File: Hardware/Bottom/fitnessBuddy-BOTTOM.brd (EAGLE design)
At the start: 33 x 33 mm, 44 parts, among them U1 AD5242-SO16, U4 PCF8523

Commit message: finished routing PPG Board
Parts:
- removed U$4: AD5171, LinnesLab-DigitalIC:SOT-23-8
- added AD5171: AD5171, LinnesLab-DigitalIC:SOT-23-8
- added C4: 100n, LinnesLab-Passives:C0603
- added LOGO1: REVISION.A, LinnesLab-Logos:REV.A
- added LOGO2: OSHW-LOGOS, LinnesLab-Logos:OSHW-LOGO-S
- moved R21 2.70 mm to (32.4, 17.4)
- moved R15 2.39 mm to (32.4, 14.0)
- moved C16 0.78 mm to (34.0, 14.0), turned to 90 degrees
- moved R13 0.30 mm to (33.4, 5.26)
- moved R19 0.30 mm to (33.4, 8.49)
- moved C18 0.18 mm to (6.77, 8.11)
- moved C17 0.16 mm to (8.66, 22.4)
- renumbered OP4 to TIA, U1 to AD5242
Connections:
- net 3.3V: now also AD5171.2, AD5171.6; no longer U$4.2, U$4.6
- net D29/LED.CTRL: now also AD5171.8; no longer U$4.8
- net GND: now also AD5171.3, C4.2; no longer U$4.3
- net N$9: now also AD5171.1, AD5171.7; no longer U$4.1, U$4.7
- net SCL: now also AD5171.4; no longer U$4.4
- net SDA: now also AD5171.5; no longer U$4.5
- net VREF: now also C4.1
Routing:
- net VREF: track 1.27 -> 35.1 mm, vias 0 -> 3
- net N$13: track 4.67 -> 13.9 mm
- net N$16: track 4.05 -> 9.17 mm
- net SCL: track 35.6 -> 39.3 mm
- net A6/TIA: track 64.9 -> 67.0 mm
- net GND: track 25.7 -> 27.6 mm, vias 14 -> 15
- net A7/PPG: track 45.4 -> 47.3 mm
- net N$8: track 0.00 -> 1.71 mm
- net PD.C: track 24.8 -> 24.3 mm

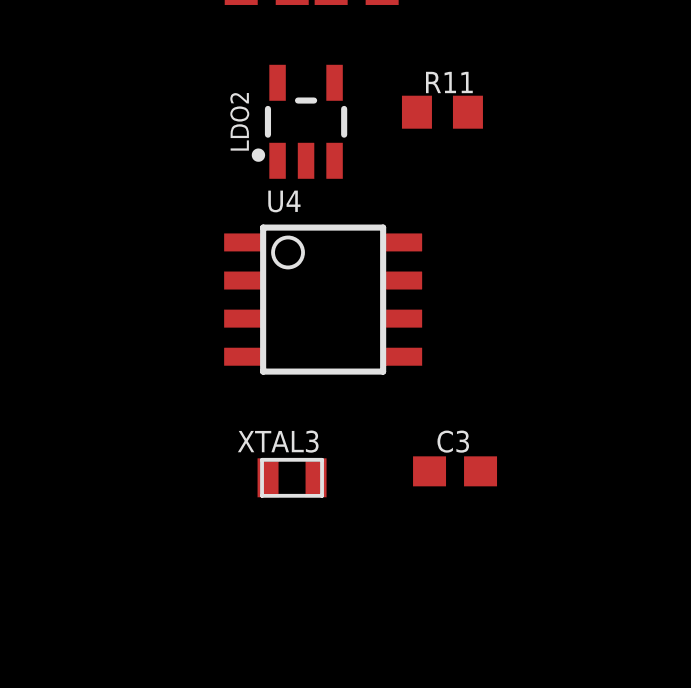
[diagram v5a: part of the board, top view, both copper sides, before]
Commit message: Began routing top board
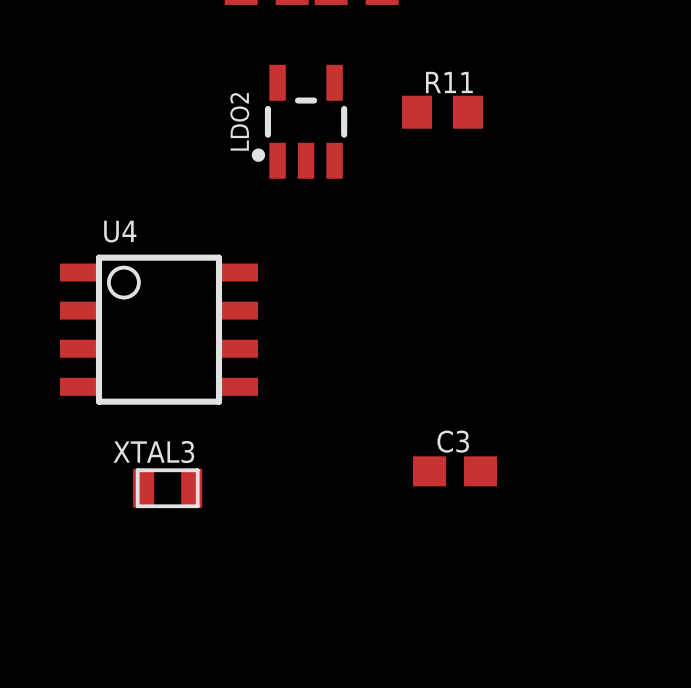
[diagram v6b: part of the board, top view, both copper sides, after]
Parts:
- moved U4 5.56 mm to (-24.3, 18.9)
- moved XTAL3 4.16 mm to (-24.0, 13.6)
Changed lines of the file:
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@@
 <drawing>
 <settings>
-<setting alwaysvectorfont="yes"/>
+<setting alwaysvectorfont="no"/>
 <setting verticaltext="up"/>
 </settings>
@@
 <attribute name="VALUE" x="-15.054578125" y="12.283440625" size="0.7112" layer="27"/>
 </element>
-<element name="XTAL3" library="LinnesLab-Clocks" package="2-SMD.NOLEAD.2.0MMTO1.2MM" package3d_urn="urn:adsk.eagle:package:18579459/2" value="32.7680kHz" x="-19.852640625" y="13.972540625" smashed="yes">
-<attribute name="NAME" x="-21.685040625" y="14.824140625" size="0.7112" layer="25"/>
-<attribute name="VALUE" x="-21.583440625" y="12.277340625" size="0.7112" layer="27"/>
-</element>
-<element name="U4" library="LinnesLab-Clocks" package="SO8" package3d_urn="urn:adsk.eagle:package:18599600/2" value="PCF8523" x="-18.81631875" y="19.9136" smashed="yes">
-<attribute name="DIGIKEY" value="568-5306-1-ND" x="-29.6291" y="23.8506" size="1.778" layer="27" display="off"/>
-<attribute name="I2C_ADDRESS" value="0x68h" x="-29.6291" y="23.8506" size="1.778" layer="27" display="off"/>
-<attribute name="MFN" value="PCF8523T/1,118" x="-29.6291" y="23.8506" size="1.778" layer="27" display="off"/>
-<attribute name="MFN_MANUFACTURER" value="NXP USA Inc." x="-29.6291" y="23.8506" size="1.778" layer="27" display="off"/>
-<attribute name="NAME" x="-20.72131875" y="22.8346" size="0.7112" layer="25"/>
-<attribute name="VALUE" x="-20.72131875" y="16.3576" size="0.7112" layer="27"/>
+<element name="XTAL3" library="LinnesLab-Clocks" package="2-SMD.NOLEAD.2.0MMTO1.2MM" package3d_urn="urn:adsk.eagle:package:18579459/2" value="32.7680kHz" x="-23.997921875" y="13.624559375" smashed="yes">
+<attribute name="NAME" x="-25.830321875" y="14.476159375" size="0.7112" layer="25"/>
+<attribute name="VALUE" x="-25.728721875" y="11.929359375" size="0.7112" layer="27"/>
+</element>
+<element name="U4" library="LinnesLab-Clocks" package="SO8" package3d_urn="urn:adsk.eagle:package:18599600/2" value="PCF8523" x="-24.287478125" y="18.9103" smashed="yes">
+<attribute name="DIGIKEY" value="568-5306-1-ND" x="-35.100259375" y="22.8473" size="1.778" layer="27" display="off"/>
+<attribute name="I2C_ADDRESS" value="0x68h" x="-35.100259375" y="22.8473" size="1.778" layer="27" display="off"/>
+<attribute name="MFN" value="PCF8523T/1,118" x="-35.100259375" y="22.8473" size="1.778" layer="27" display="off"/>
+<attribute name="MFN_MANUFACTURER" value="NXP USA Inc." x="-35.100259375" y="22.8473" size="1.778" layer="27" display="off"/>
+<attribute name="NAME" x="-26.192478125" y="21.8313" size="0.7112" layer="25"/>
+<attribute name="VALUE" x="-26.192478125" y="15.3543" size="0.7112" layer="27"/>
 </element>
 <element name="C4" library="LinnesLab-Passives" package="C0603" package3d_urn="urn:adsk.eagle:package:15661989/2" value="100n" x="28.201625" y="25.68448125" smashed="yes" rot="R90">
@@
 <wire x1="-19.385278125" y1="24.539321875" x2="-15.688678125" y2="26.1594625" width="0" layer="19" extent="1-1"/>
 <wire x1="-21.54591875" y1="30.233621875" x2="-16.84871875" y2="30.233621875" width="0" layer="19" extent="1-1"/>
-<wire x1="-21.46631875" y1="18.0086" x2="-19.385278125" y2="24.539321875" width="0" layer="19" extent="1-1"/>
-<wire x1="-13.569578125" y1="14.188440625" x2="-21.46631875" y2="18.0086" width="0" layer="19" extent="1-1"/>
+<wire x1="-26.937478125" y1="17.0053" x2="-19.385278125" y2="24.539321875" width="0" layer="19" extent="1-1"/>
+<wire x1="-13.569578125" y1="14.188440625" x2="-26.937478125" y2="17.0053" width="0" layer="19" extent="1-1"/>
 <wire x1="4.75488125" y1="26.7335" x2="-15.688678125" y2="26.1594625" width="0" layer="19" extent="1-1"/>
 </signal>
@@
 <wire x1="9.506325" y1="22.435821875" x2="8.476221875" y2="21.1255625" width="0" layer="19" extent="1-1"/>
 <wire x1="-15.269578125" y1="14.188440625" x2="6.76655625" y2="7.25768125" width="0" layer="19" extent="1-1"/>
-<wire x1="-16.16631875" y1="21.8186" x2="-15.269578125" y2="14.188440625" width="0" layer="19" extent="1-1"/>
-<wire x1="-20.335278125" y1="27.139521875" x2="-16.16631875" y2="21.8186" width="0" layer="19" extent="1-1"/>
+<wire x1="-21.637478125" y1="20.8153" x2="-15.269578125" y2="14.188440625" width="0" layer="19" extent="1-1"/>
+<wire x1="-20.335278125" y1="27.139521875" x2="-21.637478125" y2="20.8153" width="0" layer="19" extent="1-1"/>
 <wire x1="-18.54871875" y1="30.233621875" x2="-20.335278125" y2="27.139521875" width="0" layer="19" extent="1-1"/>
 <wire x1="-13.988678125" y1="39.0880625" x2="-18.54871875" y2="30.233621875" width="0" layer="19" extent="1-1"/>
@@
 <wire x1="2.99211875" y1="18.7727625" x2="2.99211875" y2="5.087621875" width="0.1524" layer="1"/>
 <wire x1="7.176221875" y1="18.7727625" x2="2.99211875" y2="18.7727625" width="0.1524" layer="1"/>
-<wire x1="-16.16631875" y1="18.0086" x2="7.176221875" y2="18.7727625" width="0" layer="19" extent="1-1"/>
+<wire x1="-21.637478125" y1="17.0053" x2="7.176221875" y2="18.7727625" width="0" layer="19" extent="1-1"/>
 </signal>
 <signal name="SCL">
@@
 <wire x1="7.176221875" y1="21.1255625" x2="3.64425625" y2="21.1255625" width="0.1524" layer="1"/>
 <wire x1="3.64425625" y1="21.1255625" x2="3.57351875" y2="21.1963" width="0.1524" layer="1"/>
-<wire x1="-16.16631875" y1="19.2786" x2="3.57351875" y2="19.99488125" width="0" layer="19" extent="1-1"/>
+<wire x1="-21.637478125" y1="18.2753" x2="3.57351875" y2="19.99488125" width="0" layer="19" extent="1-1"/>
 </signal>
 <signal name="A6/TIA">
@@
 <contactref element="XTAL3" pad="P$1"/>
 <contactref element="U4" pad="2"/>
-<wire x1="-21.46631875" y1="20.5486" x2="-20.652640625" y2="13.972540625" width="0" layer="19" extent="1-1"/>
+<wire x1="-26.937478125" y1="19.5453" x2="-24.797921875" y2="13.624559375" width="0" layer="19" extent="1-1"/>
 </signal>
 <signal name="N$6">
 <contactref element="XTAL3" pad="P$2"/>
 <contactref element="U4" pad="1"/>
-<wire x1="-21.46631875" y1="21.8186" x2="-19.052640625" y2="13.972540625" width="0" layer="19" extent="1-1"/>
+<wire x1="-26.937478125" y1="20.8153" x2="-23.197921875" y2="13.624559375" width="0" layer="19" extent="1-1"/>
 </signal>
 <signal name="VBATT">

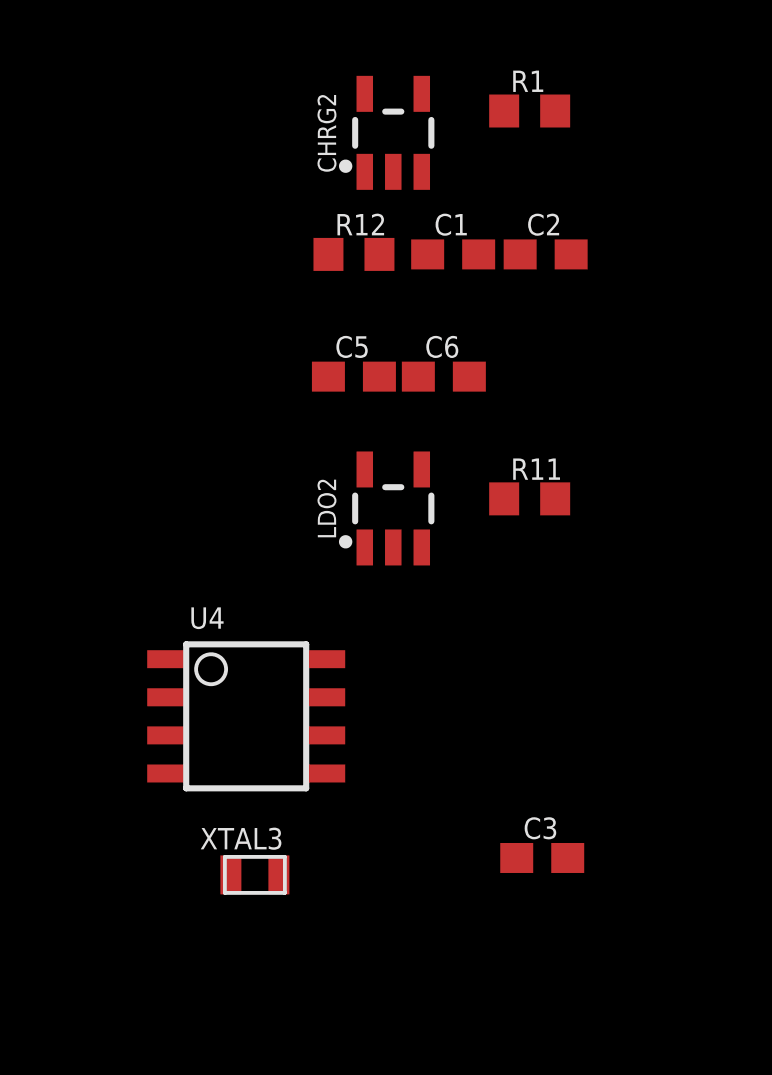
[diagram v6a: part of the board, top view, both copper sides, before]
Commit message: routed top board
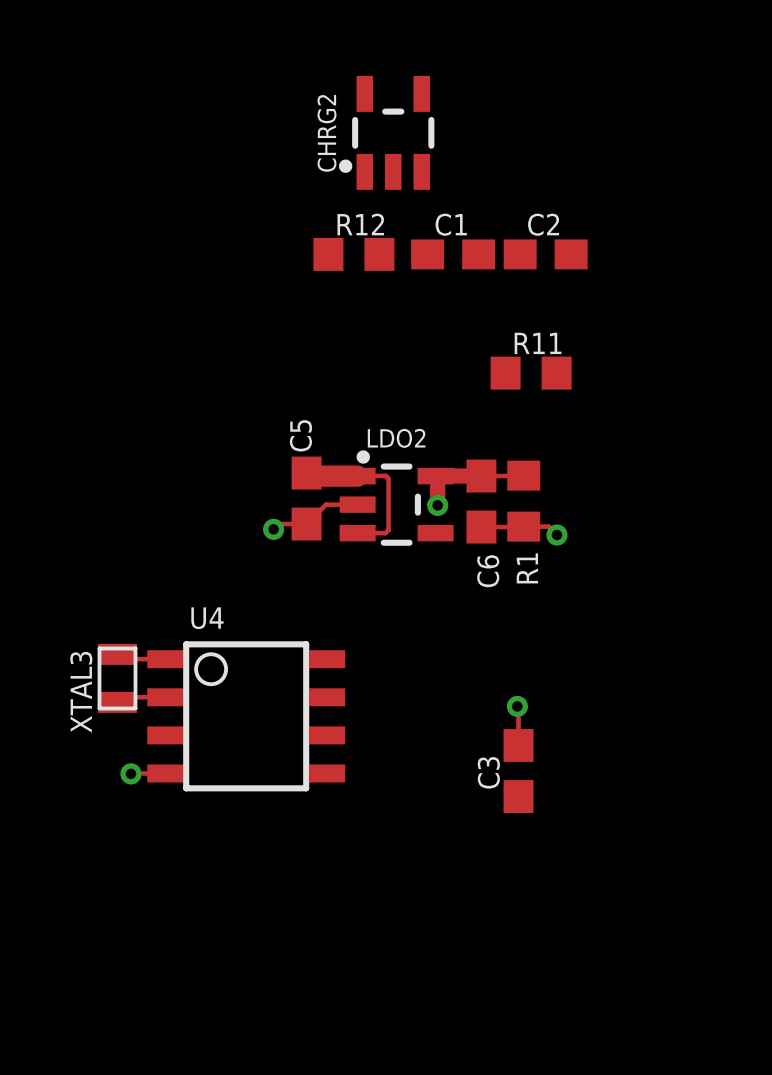
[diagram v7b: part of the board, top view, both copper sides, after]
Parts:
- moved R1 13.0 mm to (-15.0, 26.1), turned to 90 degrees
- moved XTAL3 7.99 mm to (-28.6, 20.2), turned to 90 degrees
- moved C5 4.36 mm to (-22.3, 26.2), turned to 90 degrees
- moved C6 4.35 mm to (-16.4, 26.1), turned to 270 degrees
- moved R11 4.19 mm to (-14.8, 30.4)
- moved C3 3.00 mm to (-15.2, 17.1), turned to 90 degrees
- moved LDO2 0.17 mm to (-19.3, 26.0), turned to 270 degrees
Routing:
- net GND: track 27.6 -> 35.9 mm, vias 15 -> 19
- net VIN: track 0.00 -> 5.60 mm
- net 3.3V: track 1.32 -> 5.60 mm, vias 0 -> 1
- net N$5: track 0.00 -> 1.71 mm
- net N$6: track 0.00 -> 1.71 mm

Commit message: Reorganized top and bottom boards, went back and rerouted some of top board (basically did take 005 and take 006)
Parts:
- moved C1 8.13 mm to (-19.3, 42.2)
- moved R12 6.81 mm to (-16.8, 39.9), turned to 270 degrees
- moved C2 5.51 mm to (-19.4, 36.3), turned to 180 degrees
- moved R11 4.54 mm to (-12.8, 34.4), turned to 180 degrees
- moved CHRG2 1.04 mm to (-19.4, 39.4), turned to 180 degrees
- moved C6 0.37 mm to (-16.7, 26.3)
- moved LDO2 0.37 mm to (-19.5, 26.2)
- moved C5 0.37 mm to (-22.5, 26.4)
- moved R1 0.37 mm to (-15.3, 26.3)
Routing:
- net N$4: track 0.00 -> 6.72 mm
- net VIN: track 5.60 -> 7.40 mm
- net D27/CHRG.STATUS: track 0.00 -> 1.69 mm
- net VLIPO: track 0.00 -> 1.58 mm
